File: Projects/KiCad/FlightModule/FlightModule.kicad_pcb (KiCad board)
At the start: 2 copper layers, 110 x 95 mm, 50 parts, among them J1 Conn_01x04_Pin, J2 Conn_01x04_Socket, J3 Conn_01x02_Pin, J4 Conn_01x02_Pin, J5 Conn_01x02_Pin, J6 Conn_01x02_Pin, Q2 DTC143E, SW1 SW_Push, U1 NUCLEO-F303K8, U2 MCP2562-E-P, U3 TLP222A, U4 TLP222A, U5 24LC1025, U6 24LC1025

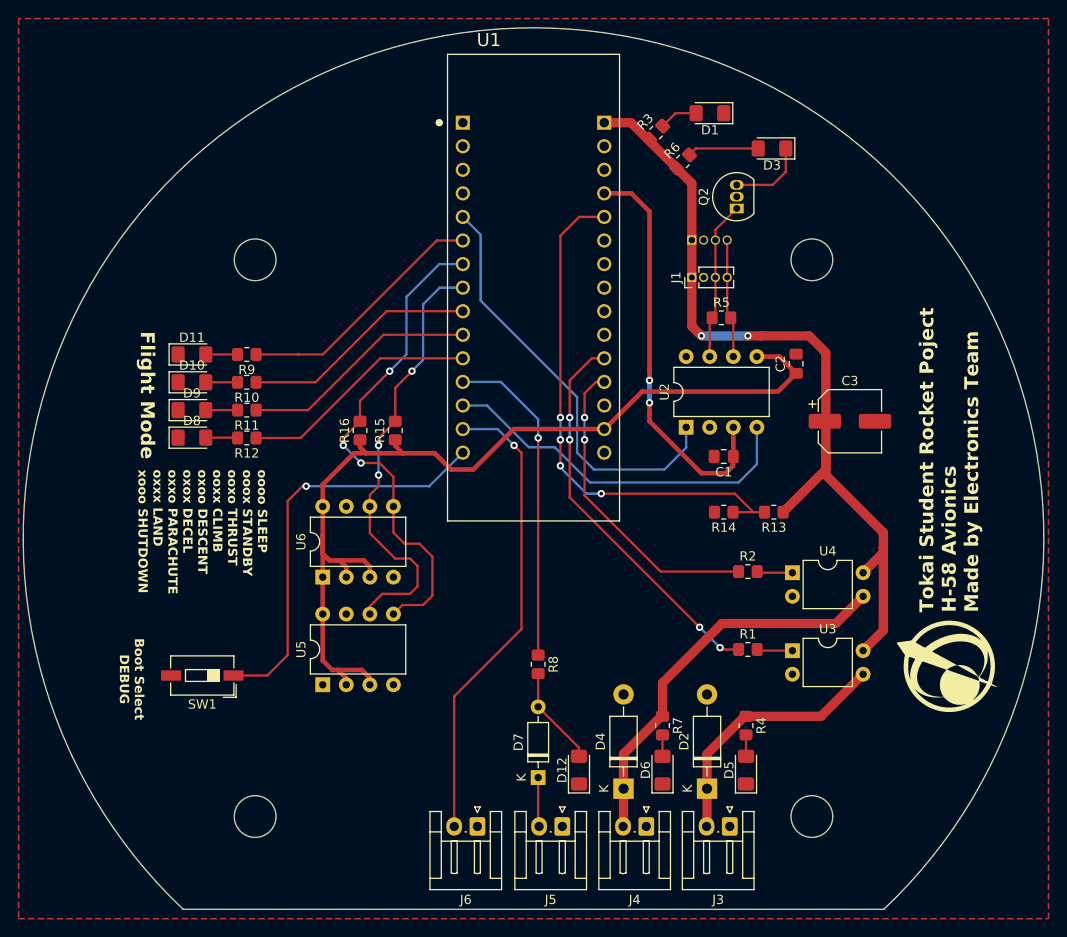
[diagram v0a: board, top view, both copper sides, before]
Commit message: バスパワーのピンヘッダをP1.27からP2.54に修正
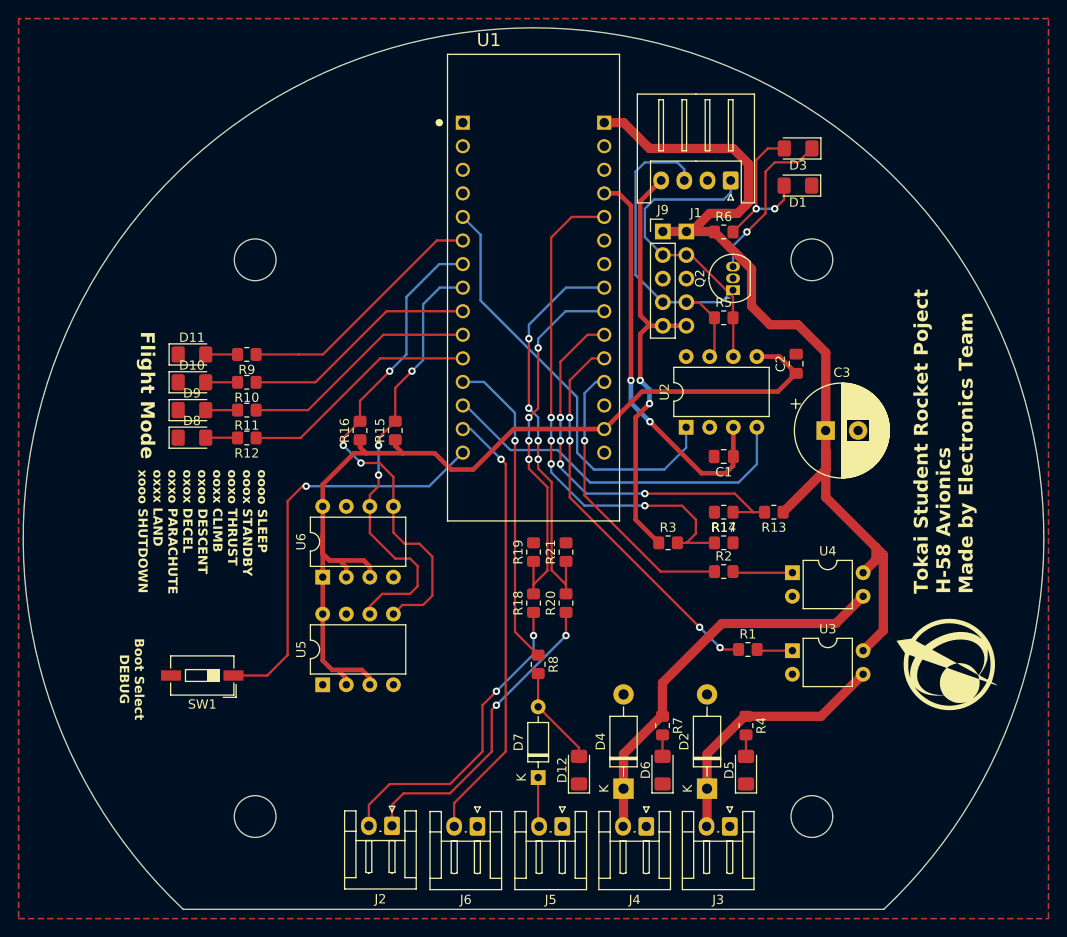
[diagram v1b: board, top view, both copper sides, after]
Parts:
- added J10: Conn_01x05_Socket, Connector_PinSocket_2.54mm:PinSocket_1x05_P2.54mm_Vertical, B.Cu at (165.0, 72.0)
- added J9: Conn_01x05_Pin, Connector_PinHeader_2.54mm:PinHeader_1x05_P2.54mm_Vertical, F.Cu at (162.4, 72.0)
- added R17: ?Ω, Resistor_SMD:R_0805_2012Metric_Pad1.20x1.40mm_HandSolder, F.Cu at (169.0, 105.5)
- added R18: ?Ω, Resistor_SMD:R_0805_2012Metric_Pad1.20x1.40mm_HandSolder, F.Cu at (148.5, 112.0)
- added R19: ?Ω, Resistor_SMD:R_0805_2012Metric_Pad1.20x1.40mm_HandSolder, F.Cu at (148.5, 106.5)
- added R20: ?Ω, Resistor_SMD:R_0805_2012Metric_Pad1.20x1.40mm_HandSolder, F.Cu at (152.0, 112.0)
- added R21: ?Ω, Resistor_SMD:R_0805_2012Metric_Pad1.20x1.40mm_HandSolder, F.Cu at (152.0, 106.5)
- C3: value 220μF -> 470μF; footprint Capacitor_SMD:CP_Elec_6.3x7.7 -> Capacitor_THT:CP_Radial_D10.0mm_P3.50mm
- J1: footprint Connector_PinHeader_1.27mm:PinHeader_1x04_P1.27mm_Vertical -> Connector_JST:JST_XH_S4B-XH-A_1x04_P2.50mm_Horizontal
- J2: value Conn_01x04_Socket -> Conn_01x02_Pin; footprint Connector_PinSocket_1.27mm:PinSocket_1x04_P1.27mm_Vertical -> Connector_JST:JST_EH_S2B-EH_1x02_P2.50mm_Horizontal; moved to F.Cu
- R3: value 2kΩ -> ?Ω
- moved J2 70.9 mm to (133.2, 136.0), turned to 180 degrees
- moved R3 44.2 mm to (163.0, 105.5), turned to 0 degrees
- moved D1 12.3 mm to (177.0, 67.0)
- moved J1 11.3 mm to (169.8, 66.5), turned to 180 degrees
- moved Q2 8.81 mm to (170.0, 78.3)
- moved R6 8.78 mm to (169.0, 72.0), turned to 0 degrees
- moved D3 2.81 mm to (177.0, 63.0)
- moved C3 2.80 mm to (180.0, 93.4)
- moved R2 2.60 mm to (169.0, 108.6)
- moved R5 0.25 mm to (169.0, 81.2)
- moved G*** 0.20 mm to (193.0, 118.6)
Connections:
- D3 pad 2: Net-(D3-A) -> Net-(D1-A)
- J1 pad 1: SOLENOID_POWER -> CAN_L
- J1 pad 4: CAN_L -> +5V
- J2 pad 1: SOLENOID_POWER -> Net-(J2-Pin_1)
- J2 pad 2: GND -> Net-(J2-Pin_2)
- R13 pad 2: VOLTAGE -> VOLTAGE_12V
- R14 pad 1: VOLTAGE -> VOLTAGE_12V
- R3 pad 1: SOLENOID_POWER -> +5V
- R3 pad 2: Net-(D1-A) -> VOLTAGE_5V
- R6 pad 2: Net-(D3-A) -> Net-(D1-A)
- U1 pad 4_10: unconnected-(U1B-PA3-Pad4_10) -> VOLTAGE_12V
- U1 pad 4_5: VOLTAGE -> VOLTAGE_5V
- U1 pad 4_8: unconnected-(U1B-PA5-Pad4_8) -> VOLTAGE_18V
- U1 pad 4_9: unconnected-(U1B-PA4-Pad4_9) -> VOLTAGE_15V
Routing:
- net VOLTAGE: track 56.7 -> 0.00 mm, vias 4 -> 0
- net VOLTAGE_5V: track 0.00 -> 56.6 mm, vias 0 -> 4
- net +5V: track 44.1 -> 90.3 mm, vias 2 -> 4
- net VOLTAGE_12V: track 0.00 -> 43.5 mm, vias 0 -> 4
- net VOLTAGE_18V: track 0.00 -> 43.0 mm, vias 0 -> 4
- net VOLTAGE_15V: track 0.00 -> 40.2 mm, vias 0 -> 4
- net Net-(J2-Pin_2): track 0.00 -> 34.2 mm, vias 0 -> 2
- net Net-(J2-Pin_1): track 0.00 -> 33.7 mm, vias 0 -> 2
- net CAN_H: track 17.2 -> 38.7 mm
- net CAN_L: track 12.8 -> 32.6 mm
- net Net-(D1-A): track 4.18 -> 17.2 mm, vias 0 -> 2
- net SOLENOID_POWER: track 90.9 -> 102.3 mm, vias 2 -> 0
- net Net-(D3-K): track 8.39 -> 17.7 mm, vias 0 -> 1
- net Net-(D3-A): track 7.69 -> 0.00 mm
- net FLIGHT_PIN: track 50.7 -> 47.5 mm
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
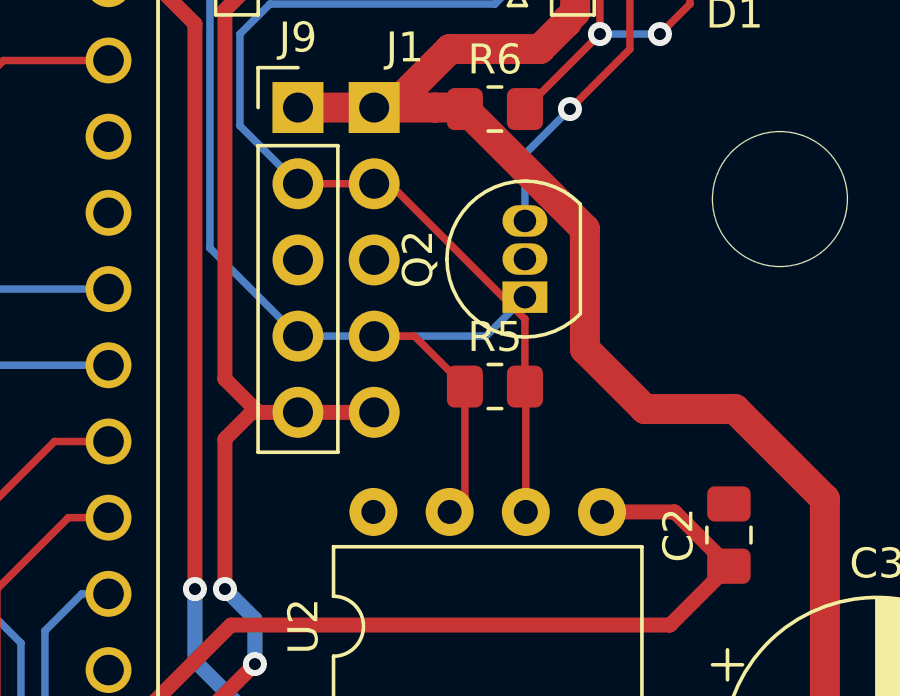
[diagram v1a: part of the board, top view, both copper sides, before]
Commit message: バスパワーの接続を修正
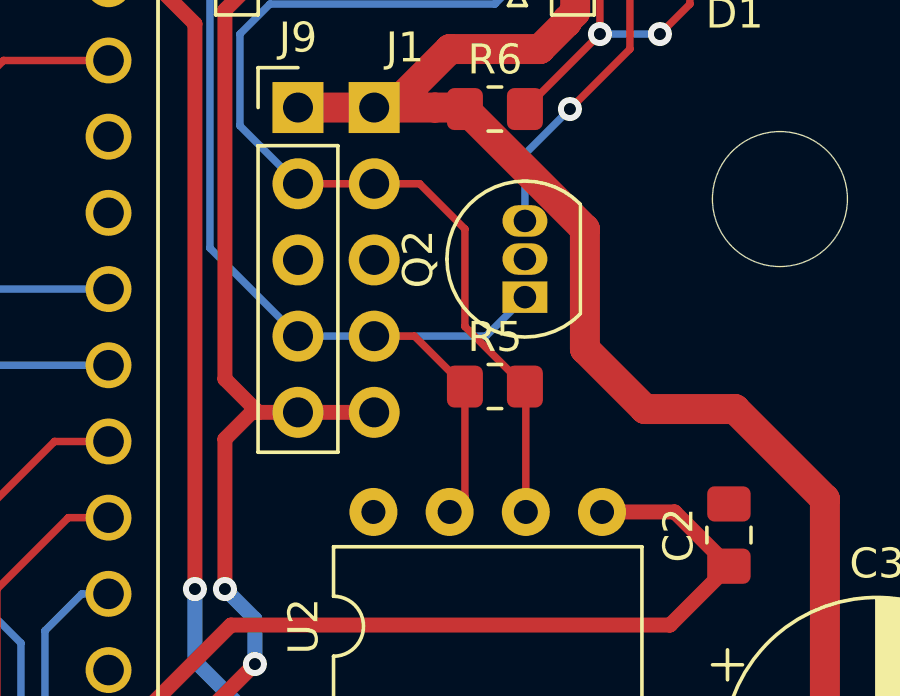
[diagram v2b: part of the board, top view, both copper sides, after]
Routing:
- net CAN_L: track 32.6 -> 33.5 mm

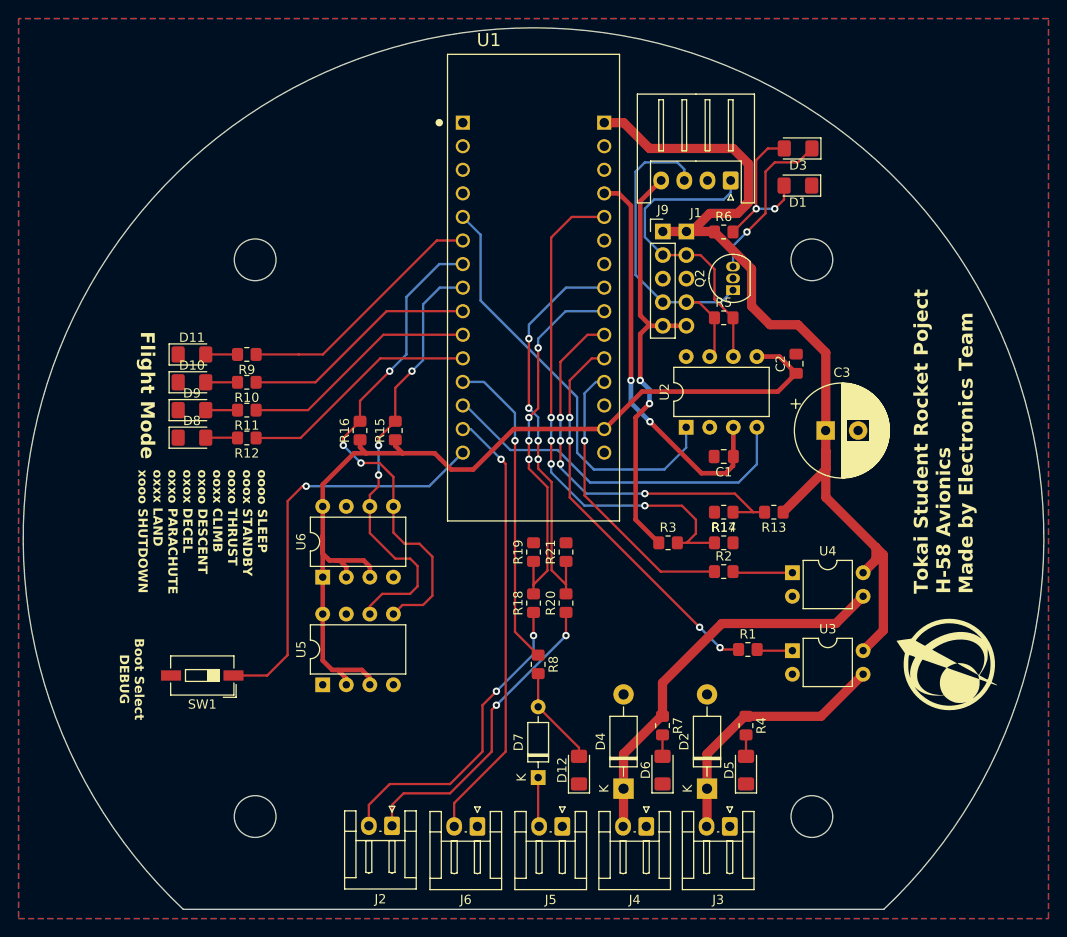
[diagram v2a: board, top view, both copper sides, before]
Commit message: RCを解決
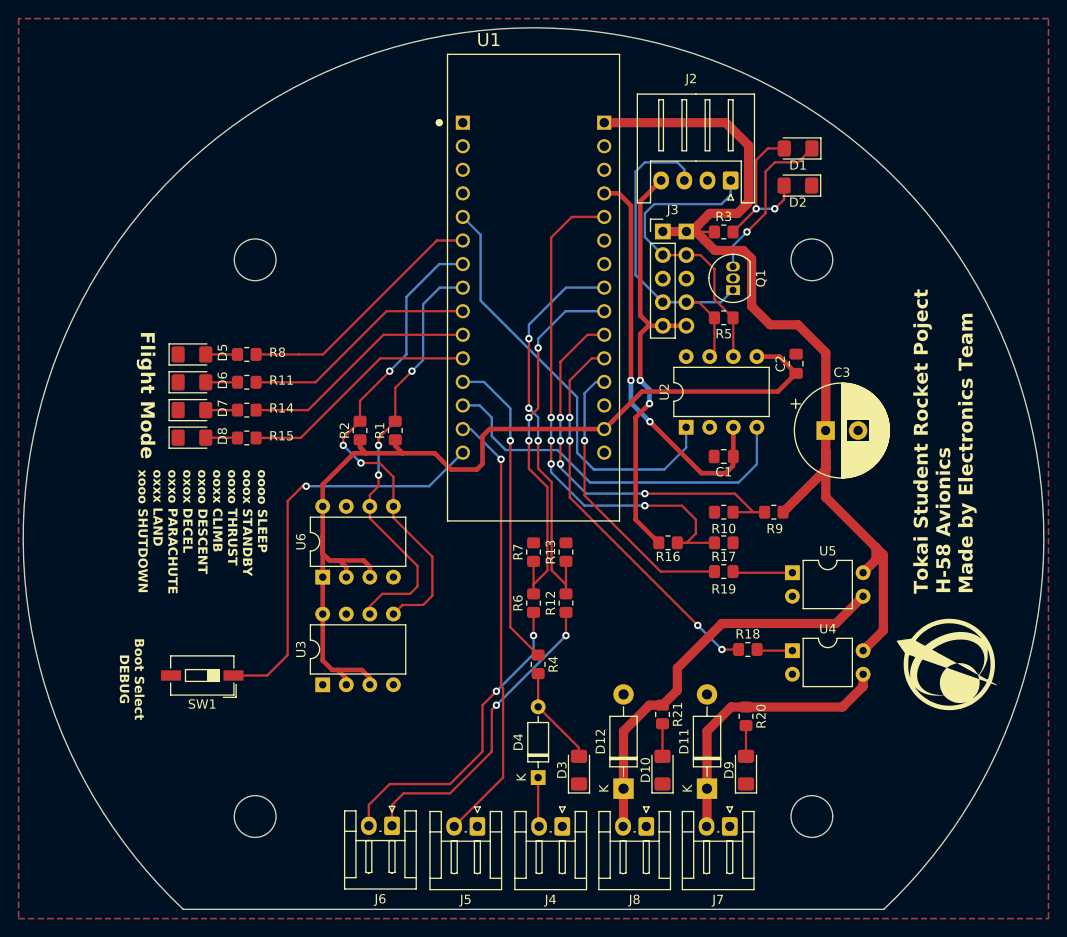
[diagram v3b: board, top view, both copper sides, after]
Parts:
- moved R21 1.20 mm to (162.4, 124.0)
- moved R20 1.00 mm to (171.4, 124.2)
- renumbered D3 to D1, D6 to D10, D2 to D11, D4 to D12, D1 to D2, D12 to D3, D7 to D4, D11 to D5, D10 to D6, D9 to D7, D5 to D9, J10 to J1, J1 to J2, J9 to J3, J5 to J4, J6 to J5, J2 to J6, J3 to J7, J4 to J8, Q2 to Q1, R15 to R1, R14 to R10, R10 to R11, R20 to R12, R21 to R13, R11 to R14, R12 to R15, R3 to R16, R1 to R18, R2 to R19, R16 to R2, R4 to R20, R7 to R21, R6 to R3, R8 to R4, R18 to R6, R19 to R7, R9 to R8, R13 to R9, U5 to U3, U3 to U4, U4 to U5
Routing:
- net SOLENOID_POWER: track 102.3 -> 106.1 mm
- net Net-(D11-K): track 28.2 -> 30.4 mm
- net +3.3V: track 104.6 -> 106.4 mm
- net Net-(D10-A): track 2.31 -> 3.51 mm
- net CAN_RX: track 39.9 -> 41.1 mm
- net Net-(D9-A): track 2.31 -> 3.31 mm
- net I2C_SDA: track 53.7 -> 52.7 mm
- net I2C_SCL: track 47.7 -> 46.8 mm
- net Net-(D12-K): track 42.8 -> 43.5 mm
- net VOLTAGE_18V: vias 4 -> 3
- net VOLTAGE_15V: vias 4 -> 3

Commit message: 計測モジュールとフライトモジュール終わり
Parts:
- removed the D1 at (177.0, 63.0)
- removed Q1: DTC143E, Package_TO_SOT_THT:TO-92_Inline
- removed the R1 at (133.6, 93.4)
- removed the R2 at (129.8, 93.4)
- removed the U3 at (125.8, 120.8)
- removed U6: 24LC1025, Package_DIP:DIP-8_W7.62mm
- added D8: LED, LED_SMD:LED_1206_3216Metric_Pad1.42x1.75mm_HandSolder, F.Cu at (130.0, 61.0)
- added D9: LED, LED_SMD:LED_1206_3216Metric_Pad1.42x1.75mm_HandSolder, F.Cu at (130.0, 68.5)
- added R14: 100Ω, Resistor_SMD:R_0805_2012Metric_Pad1.20x1.40mm_HandSolder, F.Cu at (133.5, 61.0)
- added R15: 100Ω, Resistor_SMD:R_0805_2012Metric_Pad1.20x1.40mm_HandSolder, F.Cu at (133.5, 68.5)
- added R18: 4.7kΩ, Resistor_SMD:R_0805_2012Metric_Pad1.20x1.40mm_HandSolder, F.Cu at (131.0, 103.0)
- added SW2: SW_Push, Button_Switch_THT:SW_PUSH_6mm, F.Cu at (111.2, 121.8)
- added U5: MB85RS2MT, Package_DIP:DIP-8_W7.62mm, F.Cu at (129.9, 107.4)
- J4, J7, J8: footprint Connector_JST:JST_EH_S2B-EH_1x02_P2.50mm_Horizontal -> Hirose_Connector:Hirose_DF1B
- J5: renamed from J6; footprint Connector_JST:JST_EH_S2B-EH_1x02_P2.50mm_Horizontal -> Hirose_Connector:Hirose_DF1B
- J6: renamed from J5; footprint Connector_JST:JST_EH_S2B-EH_1x02_P2.50mm_Horizontal -> Hirose_Connector:Hirose_DF1B
- SW1: footprint Button_Switch_SMD:SW_DIP_SPSTx01_Slide_6.7x4.1mm_W6.73mm_P2.54mm_LowProfile_JPin -> Button_Switch_THT:SW_PUSH_6mm
- moved SW1 6.73 mm to (111.2, 113.2), turned to 0 degrees
- moved D2 4.52 mm to (153.0, 125.5)
- moved C3 4.10 mm to (180.0, 97.5)
- moved D12 3.92 mm to (167.2, 128.1)
- moved D13 3.92 mm to (158.2, 128.1)
- moved D10 3.49 mm to (171.4, 126.5)
- moved D11 3.49 mm to (162.4, 126.5)
- moved R21 3.20 mm to (171.4, 121.0)
- moved J7 3.15 mm to (166.5, 136.0), turned to 0 degrees
- moved J8 3.15 mm to (157.5, 136.0), turned to 0 degrees
- moved J4 3.10 mm to (148.5, 136.0), turned to 0 degrees
- moved R22 3.00 mm to (162.4, 121.0)
- moved D3 2.99 mm to (149.0, 127.8)
- moved J6 2.95 mm to (139.5, 136.0), turned to 0 degrees
- moved J5 2.75 mm to (130.5, 136.0), turned to 0 degrees
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- renumbered D2 to D1, D9 to D10, D10 to D11, D11 to D12, D12 to D13, D3 to D2, D4 to D3, D5 to D4, D6 to D5, D7 to D6, D8 to D7, R3 to R1, R14 to R10, R9 to R11, R10 to R12, R15 to R13, R18 to R19, R4 to R2, R19 to R20, R20 to R21, R21 to R22, R5 to R3, R6 to R4, R7 to R5, R12 to R6, R13 to R7, R11 to R9, U4 to U3, U5 to U4
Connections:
- J5 pad 1: Net-(J6-Pin_1) -> Net-(J5-Pin_1)
- J5 pad 2: Net-(J6-Pin_2) -> Net-(J5-Pin_2)
- R4 pad 1: Net-(J6-Pin_2) -> Net-(J5-Pin_1)
- R6 pad 1: Net-(J6-Pin_1) -> Net-(J5-Pin_2)
- SW1 pad 1: DEBUG_MODE -> GND
- SW1 pad 2: GND -> DEBUG_MODE
- U1 pad 3_1: unconnected-(U1A-PA9-Pad3_1) -> CAN_RECEIVE_STATUS
- U1 pad 3_2: unconnected-(U1A-PA10-Pad3_2) -> CAN_SEND_STATUS
- U1 pad 3_7: I2C_SDA -> SPI_CS_FRAM
- U1 pad 3_8: I2C_SCL -> DUMP_MODE
- U1 pad 4_10: VOLTAGE_12V -> VOLTAGE_15V
- U1 pad 4_11: CONTROL_SEPARATOR_0 -> VOLTAGE_5V
- U1 pad 4_15: unconnected-(U1B-PB3-Pad4_15) -> CONTROL_SEPARATOR_0
- U1 pad 4_5: VOLTAGE_5V -> VOLTAGE_12V
- U1 pad 4_6: unconnected-(U1B-PA7-Pad4_6) -> SPI_MOSI
- U1 pad 4_7: unconnected-(U1B-PA6-Pad4_7) -> SPI_MISO
- U1 pad 4_8: VOLTAGE_18V -> SPI_SCLK
- U1 pad 4_9: VOLTAGE_15V -> VOLTAGE_18V
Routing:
- net DUMP_MODE: track 0.00 -> 67.2 mm, vias 0 -> 1
- net SPI_MOSI: track 0.00 -> 53.0 mm, vias 0 -> 1
- net I2C_SDA: track 52.7 -> 0.00 mm, vias 3 -> 0
- net SPI_MISO: track 0.00 -> 47.3 mm, vias 0 -> 1
- net I2C_SCL: track 46.8 -> 0.00 mm, vias 3 -> 0
- net SPI_SCLK: track 0.00 -> 46.4 mm, vias 0 -> 1
- net +3.3V: track 106.4 -> 64.1 mm
- net GND: track 0.00 -> 40.2 mm, vias 0 -> 98
- net SPI_CS_FRAM: track 0.00 -> 37.8 mm, vias 0 -> 1
- net Net-(J6-Pin_2): track 34.2 -> 0.00 mm, vias 2 -> 0
- net Net-(J6-Pin_1): track 33.7 -> 0.00 mm, vias 2 -> 0
- net Net-(J5-Pin_1): track 0.00 -> 30.2 mm, vias 0 -> 2
- net Net-(J5-Pin_2): track 0.00 -> 29.9 mm, vias 0 -> 2
- net Net-(D1-K): track 17.7 -> 0.00 mm, vias 1 -> 0
- net VOLTAGE_5V: track 56.6 -> 40.7 mm
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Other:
- board text added: "15V"
- board text added: "18V"
- board text added: "Boot Selection"
- board text added: "CAMERA"
- board text added: "CAN"
- board text added: "DEBUG"
- board text added: "DUMP"
- board text added: "Made by Electronics Team 2023"
- board text added: "PIN"
- board text added: "POWER"
- board text added: "RECEIVE"
- board text added: "SEND"
- board text added: "SEPA1"
- board text added: "SEPA2"
- board text added: "Tokai Student Rocket Poject H-58 Avionics"
- board text added: "VREF"
- board text removed: "Boot Select DEBUG"
- board text removed: "Tokai Student Rocket Poject H-58 Avionics Made by Electronics Team"

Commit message: 全モジュールのkicadを一通り作った
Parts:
- moved G*** 5.92 mm to (192.5, 124.5)
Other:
- board text added: "CAN-BUS < TERMINATION RESISTOR (OPTIONAL)"
